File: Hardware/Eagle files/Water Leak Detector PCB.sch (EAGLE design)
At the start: 28 parts, among them IC1 74AHCT125, J1 Sensor 1, J2 Sensor 2, J3 Servo

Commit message: Corrected and renamed files
Changed Photon to through hole version.  Changed the layout somewhat to
improve placement and routing.  Changed the names to be more
descriptive.
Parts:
- U$1: value PHOTON_SMD -> PHOTON_WITH_HEADERS; device Spark:PHOTON_SMD -> Spark:PHOTON_WITH_HEADERS
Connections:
- net +3.3V: now also U$1.3V3; no longer U$1G$1.3V3
- net GND: now also U$1.GND@2, U$1.GND@21; no longer U$1G$1.GND@2, U$1G$1.GND@21
- net N$11: now also U$1.D4; no longer U$1G$1.D4
- net N$14: now also U$1.D3; no longer U$1G$1.D3
- net N$16: now also U$1.A2; no longer U$1G$1.A2
- net N$17: now also U$1.D0; no longer U$1G$1.D0
- net N$19: now also U$1.D2; no longer U$1G$1.D2
- net N$2: now also U$1.A1; no longer U$1G$1.A1
- net N$22: now also U$1.D1; no longer U$1G$1.D1
- net N$23: now also U$1.D5; no longer U$1G$1.D5
- net N$3: now also U$1.A0; no longer U$1G$1.A0
- net N$4: now also U$1.D6; no longer U$1G$1.D6
- net N$7: now also U$1.A5; no longer U$1G$1.A5
- net VCC: now also U$1.VIN; no longer U$1G$1.VIN
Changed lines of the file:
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@@
 </classes>
 <parts>
-<part name="U$1" library="Spark" deviceset="PHOTON_SMD" device=""/>
 <part name="J1" library="con-lstb" deviceset="MA03-1" device="" value="Sensor 1"/>
 <part name="J2" library="con-lstb" deviceset="MA03-1" device="" value="Sensor 2"/>
@@
 <part name="GND14" library="SparkFun-Aesthetics" deviceset="GND" device=""/>
 <part name="GND15" library="SparkFun-Aesthetics" deviceset="GND" device=""/>
+<part name="U$1" library="Spark" deviceset="PHOTON" device="_WITH_HEADERS"/>
 </parts>
 <sheets>
@@
 </plain>
 <instances>
-<instance part="U$1" gate="G$1" x="-7.62" y="66.04"/>
 <instance part="J1" gate="G$1" x="-63.5" y="40.64"/>
 <instance part="J2" gate="G$1" x="-63.5" y="71.12"/>
@@
 <instance part="GND14" gate="1" x="-30.48" y="12.7" rot="MR0"/>
 <instance part="GND15" gate="1" x="-22.86" y="12.7" rot="MR0"/>
+<instance part="U$1" gate="G$1" x="-7.62" y="66.04"/>
 </instances>
 <busses>
@@
 <net name="GND" class="0">
 <segment>
-<pinref part="U$1" gate="G$1" pin="GND@2"/>
 <pinref part="JP1" gate="G$1" pin="GND"/>
 <wire x1="-25.4" y1="88.9" x2="-35.56" y2="88.9" width="0.1524" layer="91"/>
@@
 <wire x1="-68.58" y1="91.44" x2="-68.58" y2="88.9" width="0.1524" layer="91"/>
 <junction x="-68.58" y="88.9"/>
+<pinref part="U$1" gate="G$1" pin="GND@2"/>
 </segment>
 <segment>
@@
 </segment>
 <segment>
-<pinref part="U$1" gate="G$1" pin="GND@21"/>
 <pinref part="GND9" gate="1" pin="GND"/>
 <wire x1="10.16" y1="78.74" x2="22.86" y2="78.74" width="0.1524" layer="91"/>
+<pinref part="U$1" gate="G$1" pin="GND@21"/>
 </segment>
 <segment>
@@
 <wire x1="-38.1" y1="27.94" x2="-38.1" y2="63.5" width="0.1524" layer="91"/>
 <junction x="35.56" y="27.94"/>
+<wire x1="-25.4" y1="63.5" x2="-38.1" y2="63.5" width="0.1524" layer="91"/>
 <pinref part="U$1" gate="G$1" pin="A5"/>
-<wire x1="-25.4" y1="63.5" x2="-38.1" y2="63.5" width="0.1524" layer="91"/>
 </segment>
 </net>
@@
 <pinref part="R6" gate="G$1" pin="2"/>
 <junction x="30.48" y="10.16"/>
+<wire x1="10.16" y1="38.1" x2="30.48" y2="38.1" width="0.1524" layer="91"/>
 <pinref part="U$1" gate="G$1" pin="D0"/>
-<wire x1="10.16" y1="38.1" x2="30.48" y2="38.1" width="0.1524" layer="91"/>
 </segment>
 </net>
@@
 <wire x1="-53.34" y1="25.4" x2="-60.96" y2="25.4" width="0.1524" layer="91"/>
 <wire x1="-60.96" y1="25.4" x2="-60.96" y2="7.62" width="0.1524" layer="91"/>
-<pinref part="U$1" gate="G$1" pin="3V3"/>
 <wire x1="10.16" y1="93.98" x2="15.24" y2="93.98" width="0.1524" layer="91"/>
 <pinref part="J2" gate="G$1" pin="2"/>
@@
 <pinref part="C8" gate="G$1" pin="1"/>
 <junction x="-22.86" y="25.4"/>
+<pinref part="U$1" gate="G$1" pin="3V3"/>
 </segment>
 </net>
@@
 <wire x1="25.4" y1="22.86" x2="25.4" y2="48.26" width="0.1524" layer="91"/>
 <junction x="25.4" y="22.86"/>
+<wire x1="10.16" y1="48.26" x2="25.4" y2="48.26" width="0.1524" layer="91"/>
 <pinref part="U$1" gate="G$1" pin="D2"/>
-<wire x1="10.16" y1="48.26" x2="25.4" y2="48.26" width="0.1524" layer="91"/>
 </segment>
 </net>
@@
 <segment>
 <pinref part="JP1" gate="G$1" pin="VBUS"/>
-<pinref part="U$1" gate="G$1" pin="VIN"/>
 <wire x1="-86.36" y1="99.06" x2="-78.74" y2="99.06" width="0.1524" layer="91"/>
 <wire x1="-78.74" y1="99.06" x2="-68.58" y2="99.06" width="0.1524" layer="91"/>
@@
 <pinref part="C6" gate="G$1" pin="1"/>
 <junction x="-68.58" y="99.06"/>
+<pinref part="U$1" gate="G$1" pin="VIN"/>
 </segment>
 <segment>
@@
 <wire x1="33.02" y1="58.42" x2="33.02" y2="60.96" width="0.1524" layer="91"/>
 <wire x1="33.02" y1="60.96" x2="104.14" y2="60.96" width="0.1524" layer="91"/>
-<pinref part="U$1" gate="G$1" pin="D4"/>
 <wire x1="10.16" y1="58.42" x2="33.02" y2="58.42" width="0.1524" layer="91"/>
 <pinref part="MUTE" gate="G$1" pin="2"/>
+<pinref part="U$1" gate="G$1" pin="D4"/>
 </segment>
 </net>
@@
 <segment>
 <wire x1="-33.02" y1="48.26" x2="-33.02" y2="5.08" width="0.1524" layer="91"/>
-<pinref part="U$1" gate="G$1" pin="A2"/>
 <wire x1="-25.4" y1="48.26" x2="-33.02" y2="48.26" width="0.1524" layer="91"/>
 <pinref part="EXPANSION" gate="1" pin="5"/>
 <wire x1="-83.82" y1="5.08" x2="-33.02" y2="5.08" width="0.1524" layer="91"/>
+<pinref part="U$1" gate="G$1" pin="A2"/>
 </segment>
 </net>
@@
 <wire x1="12.7" y1="-5.08" x2="-45.72" y2="-5.08" width="0.1524" layer="91"/>
 <wire x1="-45.72" y1="2.54" x2="-45.72" y2="-5.08" width="0.1524" layer="91"/>
-<pinref part="U$1" gate="G$1" pin="D3"/>
 <wire x1="10.16" y1="53.34" x2="12.7" y2="53.34" width="0.1524" layer="91"/>
 <pinref part="EXPANSION" gate="1" pin="4"/>
 <wire x1="-83.82" y1="2.54" x2="-45.72" y2="2.54" width="0.1524" layer="91"/>
+<pinref part="U$1" gate="G$1" pin="D3"/>
 </segment>
 </net>
@@
 <wire x1="38.1" y1="63.5" x2="38.1" y2="93.98" width="0.1524" layer="91"/>
 <wire x1="38.1" y1="93.98" x2="40.64" y2="93.98" width="0.1524" layer="91"/>
-<pinref part="U$1" gate="G$1" pin="D5"/>
 <wire x1="10.16" y1="63.5" x2="38.1" y2="63.5" width="0.1524" layer="91"/>
 <junction x="38.1" y="63.5"/>
 <pinref part="IC1" gate="B" pin="I"/>
 <wire x1="45.72" y1="48.26" x2="38.1" y2="48.26" width="0.1524" layer="91"/>
+<pinref part="U$1" gate="G$1" pin="D5"/>
 </segment>
 </net>
@@
 <segment>
 <wire x1="27.94" y1="43.18" x2="27.94" y2="127" width="0.1524" layer="91"/>
-<pinref part="U$1" gate="G$1" pin="D1"/>
 <wire x1="10.16" y1="43.18" x2="27.94" y2="43.18" width="0.1524" layer="91"/>
 <wire x1="27.94" y1="127" x2="73.66" y2="127" width="0.1524" layer="91"/>
 <pinref part="TOGGLE" gate="G$1" pin="1"/>
+<pinref part="U$1" gate="G$1" pin="D1"/>
 </segment>
 </net>
@@
 <segment>
 <pinref part="J1" gate="G$1" pin="1"/>
+<wire x1="-55.88" y1="38.1" x2="-25.4" y2="38.1" width="0.1524" layer="91"/>
 <pinref part="U$1" gate="G$1" pin="A0"/>
-<wire x1="-55.88" y1="38.1" x2="-25.4" y2="38.1" width="0.1524" layer="91"/>
 </segment>
 </net>
 <net name="N$4" class="0">
 <segment>
-<pinref part="U$1" gate="G$1" pin="D6"/>
 <pinref part="IC1" gate="A" pin="I"/>
 <wire x1="10.16" y1="68.58" x2="33.02" y2="68.58" width="0.1524" layer="91"/>
@@
 <wire x1="33.02" y1="101.6" x2="45.72" y2="101.6" width="0.1524" layer="91"/>
 <junction x="33.02" y="68.58"/>
+<pinref part="U$1" gate="G$1" pin="D6"/>
 </segment>
 </net>
@@
 <wire x1="-55.88" y1="68.58" x2="-40.64" y2="68.58" width="0.1524" layer="91"/>
 <wire x1="-40.64" y1="68.58" x2="-40.64" y2="43.18" width="0.1524" layer="91"/>
+<wire x1="-40.64" y1="43.18" x2="-25.4" y2="43.18" width="0.1524" layer="91"/>
 <pinref part="U$1" gate="G$1" pin="A1"/>
-<wire x1="-40.64" y1="43.18" x2="-25.4" y2="43.18" width="0.1524" layer="91"/>
-</segment>
-</net>
+</segment>
+</net>

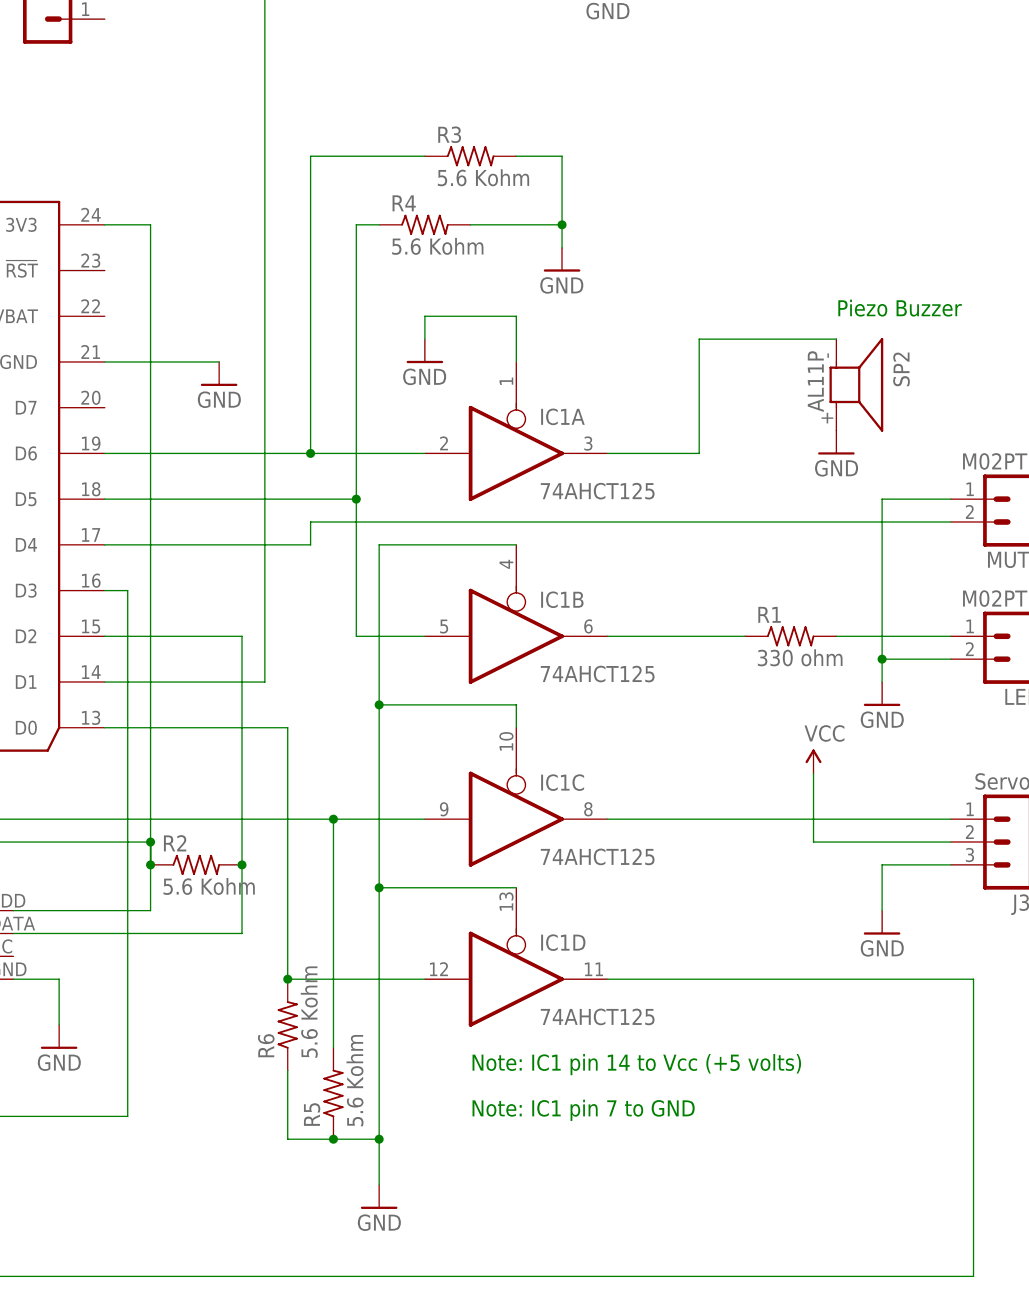
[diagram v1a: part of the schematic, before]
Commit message: Updated schematic
Updated schematic to show the resistor values for the components that
are on the parts list.
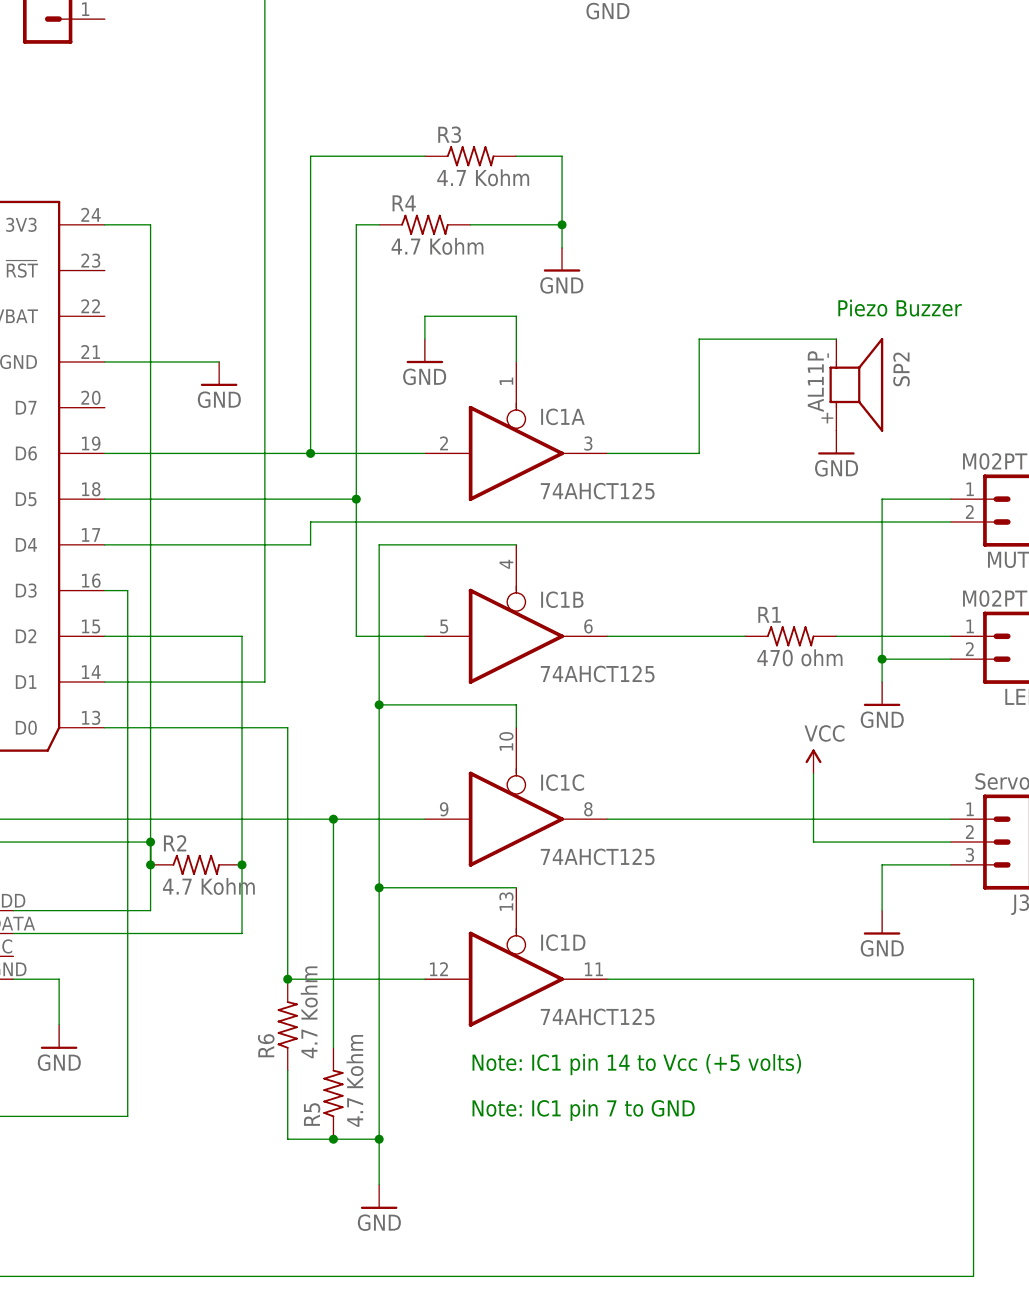
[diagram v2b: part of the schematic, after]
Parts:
- R1: value 330 ohm -> 470 ohm
- R2, R3, R4, R5, R6: value 5.6 Kohm -> 4.7 Kohm
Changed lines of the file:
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@@
 <part name="GND3" library="SparkFun-Aesthetics" deviceset="GND" device=""/>
 <part name="IC1" library="74xx-us" deviceset="74*125" device="N" value="74AHCT125"/>
-<part name="R1" library="rcl" deviceset="R-US_" device="0309/12" value="330 ohm"/>
+<part name="R1" library="rcl" deviceset="R-US_" device="0309/12" value="470 ohm"/>
 <part name="SP2" library="buzzer" deviceset="AL11P" device=""/>
 <part name="GND5" library="SparkFun-Aesthetics" deviceset="GND" device=""/>
@@
 <part name="GND4" library="SparkFun-Aesthetics" deviceset="GND" device=""/>
 <part name="GND9" library="SparkFun-Aesthetics" deviceset="GND" device=""/>
-<part name="R2" library="rcl" deviceset="R-US_" device="0309/12" value="5.6 Kohm"/>
-<part name="R3" library="rcl" deviceset="R-US_" device="0309/12" value="5.6 Kohm"/>
-<part name="R4" library="rcl" deviceset="R-US_" device="0309/12" value="5.6 Kohm"/>
-<part name="R5" library="rcl" deviceset="R-US_" device="0309/12" value="5.6 Kohm"/>
-<part name="R6" library="rcl" deviceset="R-US_" device="0309/12" value="5.6 Kohm"/>
+<part name="R2" library="rcl" deviceset="R-US_" device="0309/12" value="4.7 Kohm"/>
+<part name="R3" library="rcl" deviceset="R-US_" device="0309/12" value="4.7 Kohm"/>
+<part name="R4" library="rcl" deviceset="R-US_" device="0309/12" value="4.7 Kohm"/>
+<part name="R5" library="rcl" deviceset="R-US_" device="0309/12" value="4.7 Kohm"/>
+<part name="R6" library="rcl" deviceset="R-US_" device="0309/12" value="4.7 Kohm"/>
 <part name="C4" library="SparkFun-Passives" deviceset="CAP" device="PTH" value="0.1 uF"/>
 <part name="C5" library="SparkFun-Passives" deviceset="CAP" device="PTH" value="0.1 uF"/>
